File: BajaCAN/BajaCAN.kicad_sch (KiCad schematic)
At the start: 11 parts, among them J1 Conn_01x04, U1 AVR128DB32x-xPT, U2 MCP25625-x-SS, Y1 32.768 KHz

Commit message: Beginning work on new nodes
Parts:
- added C10, C5, C6, C7: 0.1u, symbol Device:C_Small
- added C8, C9: 4.7u, symbol Device:C_Small
- added J2: ICSP, symbol Connector_Generic:Conn_02x03_Odd_Even
- added L1: CBC2518T4R7M, symbol Device:L_Small
- added U3: MCP1603, Package_TO_SOT_SMD:TSOT-23-5_HandSoldering, symbol buck_converter:MCP1603
- added Y2: CSTNE16M0VH3C000R0, Crystal:Resonator_SMD_Murata_CSTxExxV-3Pin_3.0x1.1mm_HandSoldering, symbol Device:Resonator
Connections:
- net +5V: now also U2.1 (VIO), U2.19 (VDD), U2.27 (VDDA), C10.2, C5.2, C6.2, C7.1, C8.1, J2.2 (Pin_2), U3.1 (VIN), U3.3 (~{SHDN})
- net CAN_H: now also J1.3 (Pin_3); no longer J1.2 (Pin_2)
- net CAN_L: now also J1.4 (Pin_4); no longer J1.3 (Pin_3)
- net GND: now also J1.2 (Pin_2), C10.1, C5.1, C6.1, C7.2, J2.6 (Pin_6), Y2.2; no longer J1.4 (Pin_4)
- net MISO0: now also J2.1 (Pin_1)
- net MOSI0: now also J2.4 (Pin_4)
- net SCK0: now also J2.3 (Pin_3)
- net MCP_INT: now reaches U2.13 (~{INT})
- net MCP_INT: now also U1.12 (PD2); no longer U1.1 (PA3)
- net MCP_STBY: now reaches U2.5 (STBY)
- net MCP_STBY: now also U1.11 (PD1)
- net at U2.8 (OSC2): now also Y2.3
- net at U2.9 (OSC1): now also Y2.1
- net +3.3V: now reaches U1.10 (VDDIO2)
- net +3.3V: now also C9.1, L1.2, U3. (VFB)
- net SDA1: now reaches U1.22 (PF2)
- net SCL1: now reaches U1.23 (PF3)
- net ~{RESET}: now reaches U1.26 (~{RESET}/PF6)
- net ~{RESET}: now also J2.5 (Pin_5)
- net SDA0: now reaches U1.32 (PA2)
- new net: C8.2, C9.2, U3. (VFB)
- new net: L1.1, U3.5 (LX)
- new net SCL0: U1.1 (PA3)
- no-connect marks 0 -> 7
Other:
- note added: "3.3V"
- note added: "MVIO"
- moved on the sheet: J1

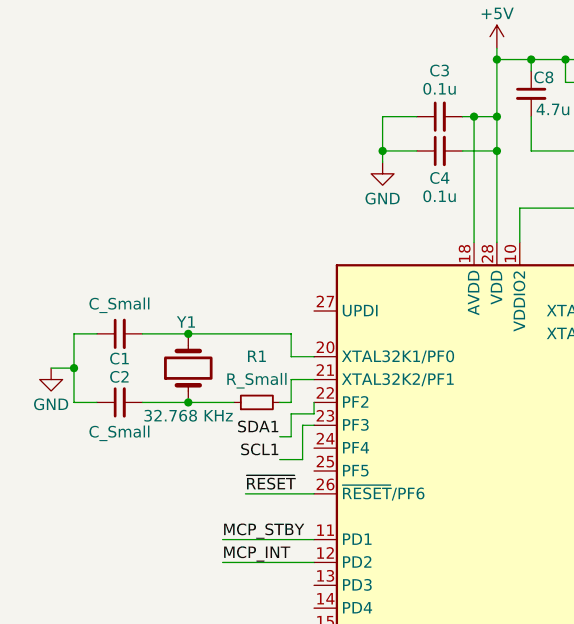
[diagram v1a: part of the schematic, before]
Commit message: A new osc symbol + footprint
Need to confirm connection for XTAL32K using square wave osc rather than xtal
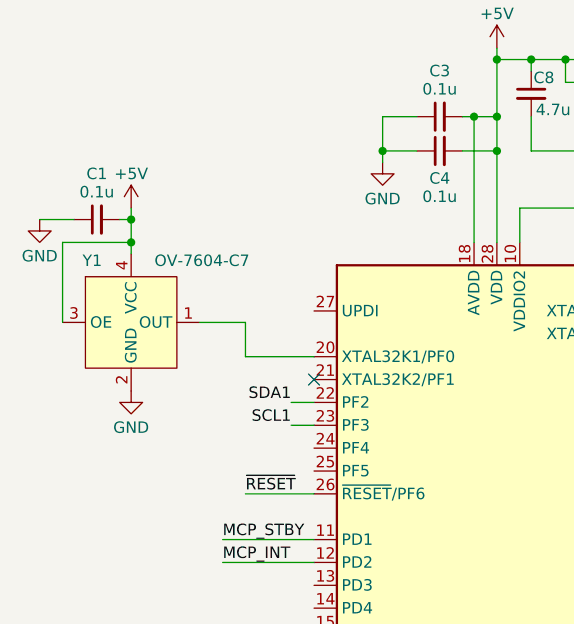
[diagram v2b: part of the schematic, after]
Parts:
- removed C2: C_Small, symbol Device:C_Small
- removed R1: R_Small, symbol Device:R_Small
- removed Y1: 32.768 KHz, symbol Device:Crystal
- added Y1: OV-7604-C7, oscillator:OV-7604-C7, symbol oscillator:OV-7604-C7
- C1: value C_Small -> 0.1u
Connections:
- net +5V: now also C1.2, Y1.3 (OE), Y1.4 (VCC)
- net GND: now also Y1.2 (GND)
- net at U1.20 (XTAL32K1/PF0): now also Y1.1 (OUT); no longer C1.2
- no-connect marks 7 -> 8
